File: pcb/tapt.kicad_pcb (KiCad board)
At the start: 4 copper layers, 28.3 x 28.3 mm, 36 parts, among them J1 Conn_01x05_Pin, J2 Conn_01x04_MountingPin, SW1 SW_SPDT_LIMIT, SW2 SW_SPST, U1 nRF52810-QCxx, Y1 32MHz, Y2 32.768kHz

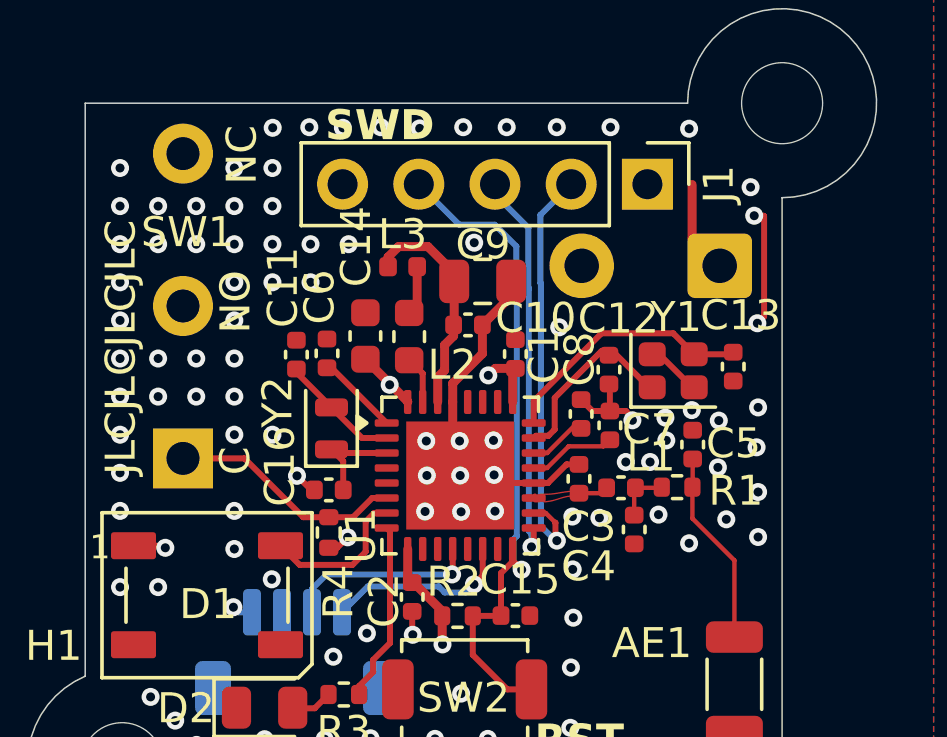
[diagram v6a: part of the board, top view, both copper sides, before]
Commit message: pcb: clock routing improvements
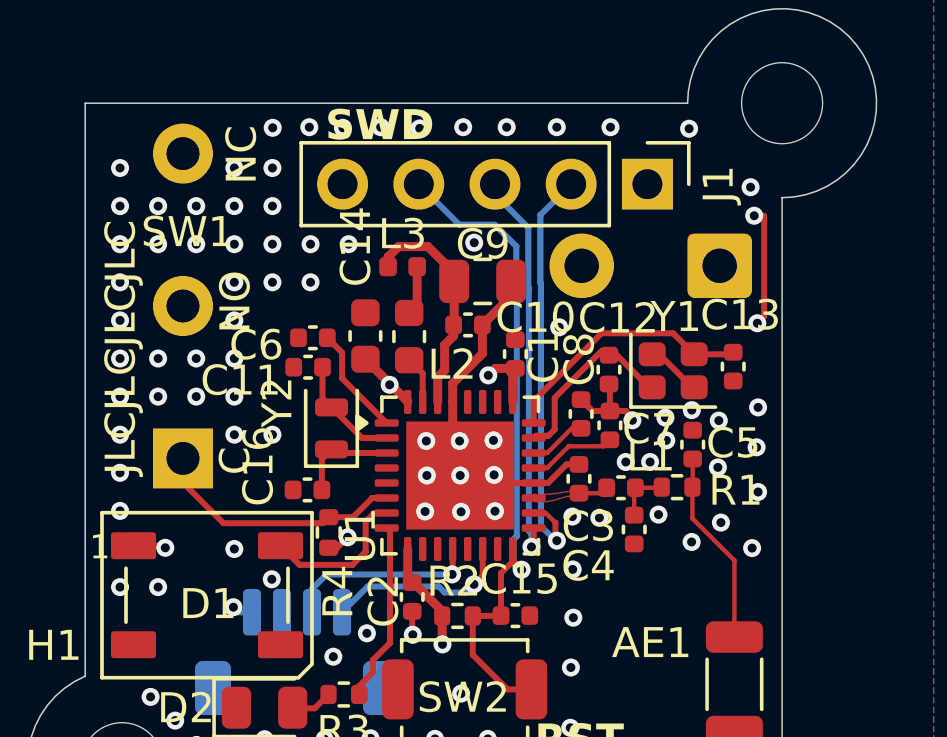
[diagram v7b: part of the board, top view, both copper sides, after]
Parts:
- moved C16 0.71 mm to (93.0, 73.3)
- moved C6 0.70 mm to (93.2, 68.3), turned to 0 degrees
- moved C11 0.57 mm to (93.0, 69.3), turned to 0 degrees
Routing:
- net VDD: track 13.2 -> 11.4 mm
- net Net-(U1-DEC1): track 2.75 -> 3.66 mm
- net GND: track 23.1 -> 22.4 mm, vias 97 -> 95
- net LIMIT: track 7.87 -> 8.51 mm
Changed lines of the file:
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@@
 	(footprint "Capacitor_SMD:C_0402_1005Metric"
 		(layer "F.Cu")
-		(at 93.66 68.8 -90)
+		(at 93.19 68.28)
 		(descr "Capacitor SMD 0402 (1005 Metric), square (rectangular) end terminal, IPC-7351 nominal, (Body size source: IPC-SM-782 page 76, https://www.pcb-3d.com/wordpress/wp-content/uploads/ipc-sm-782a_amendment_1_and_2.pdf), generated with kicad-footprint-generator")
 		(tags "capacitor")
 		(property "Reference" "C6"
-			(at -1.88 0.25 90)
+			(at -1.88 0.25 0)
 			(layer "F.SilkS")
 			(effects
@@
 		)
 		(property "Value" "100nF"
-			(at 0 1.16 90)
+			(at 0 1.16 0)
 			(layer "F.Fab")
 			(effects
@@
 		)
 		(property "Datasheet" "~"
-			(at 0 0 90)
+			(at 0 0 0)
 			(layer "F.Fab")
 			(hide yes)
@@
 		)
 		(property "Description" "Unpolarized capacitor"
-			(at 0 0 90)
+			(at 0 0 0)
 			(layer "F.Fab")
 			(hide yes)
@@
 		)
 		(property "LCSC" "C1525"
-			(at 0 0 270)
+			(at 0 0 0)
 			(unlocked yes)
 			(layer "F.Fab")
@@
 		)
 		(property "KLC_S3.3" ""
-			(at 0 0 270)
+			(at 0 0 0)
 			(unlocked yes)
 			(layer "F.Fab")
@@
 		)
 		(property "KLC_S4.1" ""
-			(at 0 0 270)
+			(at 0 0 0)
 			(unlocked yes)
 			(layer "F.Fab")
@@
 		(attr smd)
 		(fp_line
-			(start -0.107836 0.36)
-			(end 0.107836 0.36)
+			(start -0.107836 -0.36)
+			(end 0.107836 -0.36)
 			(stroke
 				(width 0.12)
@@
 		)
 		(fp_line
-			(start -0.107836 -0.36)
-			(end 0.107836 -0.36)
+			(start -0.107836 0.36)
+			(end 0.107836 0.36)
 			(stroke
 				(width 0.12)
@@
 		)
 		(fp_text user "${REFERENCE}"
-			(at 0 0 90)
+			(at 0 0 0)
 			(layer "F.Fab")
 			(effects
@@
 		)
 		(pad "1" smd roundrect
-			(at -0.48 0 270)
+			(at -0.48 0)
 			(size 0.56 0.62)
 			(layers "F.Cu" "F.Mask" "F.Paste")
@@
 		)
 		(pad "2" smd roundrect
-			(at 0.48 0 270)
+			(at 0.48 0)
 			(size 0.56 0.62)
 			(layers "F.Cu" "F.Mask" "F.Paste")
@@
 	(footprint "Capacitor_SMD:C_0402_1005Metric"
 		(layer "F.Cu")
-		(at 93.72 73.35)
+		(at 93.01 73.35)
 		(descr "Capacitor SMD 0402 (1005 Metric), square (rectangular) end terminal, IPC-7351 nominal, (Body size source: IPC-SM-782 page 76, https://www.pcb-3d.com/wordpress/wp-content/uploads/ipc-sm-782a_amendment_1_and_2.pdf), generated with kicad-footprint-generator")
 		(tags "capacitor")
@@
 	(footprint "Capacitor_SMD:C_0402_1005Metric"
 		(layer "F.Cu")
-		(at 92.64 68.84 -90)
+		(at 93.03 69.26)
 		(descr "Capacitor SMD 0402 (1005 Metric), square (rectangular) end terminal, IPC-7351 nominal, (Body size source: IPC-SM-782 page 76, https://www.pcb-3d.com/wordpress/wp-content/uploads/ipc-sm-782a_amendment_1_and_2.pdf), generated with kicad-footprint-generator")
 		(tags "capacitor")
 		(property "Reference" "C11"
-			(at -2.24 0.45 90)
+			(at -2.24 0.45 0)
 			(layer "F.SilkS")
 			(effects
@@
 		)
 		(property "Value" "12pF"
-			(at 0 1.16 90)
+			(at 0 1.16 0)
 			(layer "F.Fab")
 			(effects
@@
 		)
 		(property "Datasheet" "~"
-			(at 0 0 90)
+			(at 0 0 0)
 			(layer "F.Fab")
 			(hide yes)
@@
 		)
 		(property "Description" "Unpolarized capacitor"
-			(at 0 0 90)
+			(at 0 0 0)
 			(layer "F.Fab")
 			(hide yes)
@@
 		)
 		(property "LCSC" "C1547"
-			(at 0 0 270)
+			(at 0 0 0)
 			(unlocked yes)
 			(layer "F.Fab")
@@
 		)
 		(property "KLC_S3.3" ""
-			(at 0 0 270)
+			(at 0 0 0)
 			(unlocked yes)
 			(layer "F.Fab")
@@
 		)
 		(property "KLC_S4.1" ""
-			(at 0 0 270)
+			(at 0 0 0)
 			(unlocked yes)
 			(layer "F.Fab")
@@
 		(attr smd)
 		(fp_line
-			(start -0.107836 0.36)
-			(end 0.107836 0.36)
+			(start -0.107836 -0.36)
+			(end 0.107836 -0.36)
 			(stroke
 				(width 0.12)
@@
 		)
 		(fp_line
-			(start -0.107836 -0.36)
-			(end 0.107836 -0.36)
+			(start -0.107836 0.36)
+			(end 0.107836 0.36)
 			(stroke
 				(width 0.12)
@@
 		)
 		(fp_text user "${REFERENCE}"
-			(at 0 0 90)
+			(at 0 0 0)
 			(layer "F.Fab")
 			(effects
@@
 		)
 		(pad "1" smd roundrect
-			(at -0.48 0 270)
+			(at -0.48 0)
 			(size 0.56 0.62)
 			(layers "F.Cu" "F.Mask" "F.Paste")
@@
 		)
 		(pad "2" smd roundrect
-			(at 0.48 0 270)
+			(at 0.48 0)
 			(size 0.56 0.62)
 			(layers "F.Cu" "F.Mask" "F.Paste")
@@
 	)
 	(segment
+		(start 92.64 69.32)
+		(end 92.64 69.43)
+		(width 0.2)
+		(layer "F.Cu")
+		(net 3)
+	)
+	(segment
 		(start 103.62 70.72)
 		(end 103.09 70.72)
@@
 	)
 	(segment
-		(start 93.13 73.35)
-		(end 92.66 72.88)
-		(width 0.2)
-		(layer "F.Cu")
-		(net 3)
-	)
-	(segment
 		(start 107.9 67.9)
 		(end 108.005 67.795)
@@
 	)
 	(segment
-		(start 93.24 73.35)
-		(end 93.13 73.35)
-		(width 0.2)
-		(layer "F.Cu")
-		(net 3)
-	)
-	(segment
 		(start 98.84 68.809343)
 		(end 98.84 67.85)
@@
 	)
 	(via
-		(at 106.97 74.33)
+		(at 106.790986 74.439014)
 		(size 0.6)
 		(drill 0.3)
@@
 	)
 	(via
-		(at 90.57119 74.05)
-		(size 0.6)
-		(drill 0.3)
-		(layers "F.Cu" "B.Cu")
-		(free yes)
-		(net 3)
-	)
-	(via
 		(at 89.30119 65.16)
 		(size 0.6)
@@
 	)
 	(via
-		(at 108.03 74.92)
+		(at 107.83 75.29)
 		(size 0.6)
 		(drill 0.3)
@@
 	)
 	(via
-		(at 92.66 72.88)
-		(size 0.6)
-		(drill 0.3)
-		(layers "F.Cu" "B.Cu")
-		(net 3)
-	)
-	(via
 		(at 90.57119 67.7)
 		(size 0.6)
@@
 	)
 	(via
-		(at 105.73 75.13)
+		(at 105.814014 75.085986)
 		(size 0.6)
 		(drill 0.3)
@@
 	)
 	(segment
-		(start 105.83 63.17)
-		(end 105.83 64.96)
-		(width 0.3)
-		(layer "F.Cu")
-		(net 4)
-	)
-	(segment
 		(start 95.7675 69.8225)
 		(end 95.748643 69.841357)
@@
 	)
 	(segment
-		(start 93.66 69.28)
-		(end 93.81 69.28)
+		(start 94.164 68.774)
+		(end 94.164 69.634)
 		(width 0.2)
 		(layer "F.Cu")
@@
 	)
 	(segment
-		(start 93.81 69.28)
+		(start 94.164 69.634)
 		(end 95.65 71.12)
 		(width 0.2)
@@
 	)
 	(segment
+		(start 93.67 68.28)
+		(end 94.164 68.774)
+		(width 0.2)
+		(layer "F.Cu")
+		(net 9)
+	)
+	(segment
 		(start 97.9 66.115926)
 		(end 97.023074 65.239)
@@
 	)
 	(segment
-		(start 92.64 69.32)
-		(end 92.64 69.43)
+		(start 93.51 69.26)
+		(end 93.51 70.3)
 		(width 0.2)
 		(layer "F.Cu")
@@
 	)
 	(segment
-		(start 92.64 69.43)
+		(start 93.51 70.3)
 		(end 93.81 70.6)
 		(width 0.2)
@@
 	)
 	(segment
-		(start 93.72 74.26)
-		(end 92.87 74.26)
+		(start 95.167102 73.62)
+		(end 95.65 73.62)
 		(width 0.2)
 		(layer "F.Cu")
@@
 	)
 	(segment
-		(start 95.167102 73.62)
-		(end 95.65 73.62)
+		(start 88.86 73.11)
+		(end 88.86 72.3)
 		(width 0.2)
 		(layer "F.Cu")
@@
 	)
 	(segment
-		(start 94.527102 74.26)
-		(end 95.167102 73.62)
+		(start 90.209 74.459)
+		(end 88.86 73.11)
 		(width 0.2)
 		(layer "F.Cu")
@@
 	)
 	(segment
-		(start 92.87 74.26)
-		(end 90.91 72.3)
+		(start 93.521 74.459)
+		(end 90.209 74.459)
 		(width 0.2)
 		(layer "F.Cu")
@@
 	)
 	(segment
-		(start 90.91 72.3)
-		(end 88.86 72.3)
+		(start 94.527102 74.26)
+		(end 95.167102 73.62)
+		(width 0.2)
+		(layer "F.Cu")
+		(net 18)
+	)
+	(segment
+		(start 93.72 74.26)
+		(end 93.521 74.459)
 		(width 0.2)
 		(layer "F.Cu")
@@
 	)
 	(segment
-		(start 94.2 72.39)
-		(end 93.81 72)
+		(start 93.93 72.12)
+		(end 95.65 72.12)
 		(width 0.2)
 		(layer "F.Cu")
@@
 	)
 	(segment
-		(start 94.2 73.35)
-		(end 94.2 72.39)
+		(start 93.81 72)
+		(end 93.93 72.12)
 		(width 0.2)
 		(layer "F.Cu")
@@
 	)
 	(segment
-		(start 93.93 72.12)
-		(end 95.65 72.12)
+		(start 93.49 73.35)
+		(end 93.49 72.32)
 		(width 0.2)
 		(layer "F.Cu")
@@
 	)
 	(segment
-		(start 93.81 72)
-		(end 93.93 72.12)
+		(start 93.49 72.32)
+		(end 93.81 72)
 		(width 0.2)
 		(layer "F.Cu")
@@
 		(polygon
 			(pts
-				(xy 103.18 72.53) (xy 103 72.89) (xy 102.576996 72.986548) (xy 102.237772 72.716026) (xy 102.237772 72.282144)
-				(xy 102.576996 72.011622) (xy 103 72.10817)
+				(xy 102.57 72.75) (xy 102.47 72.91) (xy 102.256996 72.986548) (xy 101.917772 72.716026) (xy 101.917772 72.282144)
+				(xy 102.256996 72.011622) (xy 102.55 72.23)
 			)
 		)
@@
 			"394d8c8a-dd6b-4c87-8b4e-98142ac8d941" "3d8690fc-de23-45d0-94f6-2e1b3a80b6c1"
 			"3dc0b03a-ff67-4bf0-85ca-2d25956d144f" "415b4172-8e34-4346-a5c5-1051eb2f3457"
-			"5b86ad54-fa14-42c1-a748-e94901416f2a" "5d32600e-6879-4401-b099-6a89159da2ee"
-			"615a3619-708d-4502-8d74-b7aa7efaea35" "6a367b3d-0043-4cce-8e1f-52d35ba62338"
-			"6d91f0a6-c01e-44af-86f9-0d4b64dbfc3f" "70b135ad-b986-4269-b6f9-5da7b8cac3a0"
-			"7333fc35-924d-4840-92fa-a92772fa5622" "758c8fe8-1e7f-4542-b9b4-f23d3895725b"
-			"785630ad-ac58-4cdb-b5af-da5a4a5baddb" "7b16aa5f-b051-4757-a830-e2beef45a1aa"
-			"7c9397f9-86da-4db2-ac97-652ca41210de" "8e8e7b76-ae7b-4a24-9dcd-7ffe77466d64"
-			"96eed214-d4a0-4f36-a3cd-7206a8a9d089" "9feb2357-0b66-4e82-bd5d-7ee2fbd9d45f"
-			"a598a10a-4723-4f89-aa88-1a0b04a16bf2" "a7303749-ecd1-43a6-aca8-0b0743363f35"
-			"ac3cee97-7bfe-4565-9d93-5d7c506d6d97" "b7a064ec-eba1-4c6a-aef5-37707c0b57c1"
-			"cf2ff0ee-c5cc-40d8-81ca-a6bb954e566d" "d2e89277-f72c-43a6-b8d4-676bbfa7e82a"
-			"d5fe8ae3-d3a3-4ef5-a2d5-cf467fb21f55" "d7f734d0-b082-438e-baf6-68e1a54f13b6"
-			"dc391ced-6002-4562-9dd1-63ed992c9425" "f134cc32-a03e-4154-9756-2d59eb056f0c"
+			"5d32600e-6879-4401-b099-6a89159da2ee" "615a3619-708d-4502-8d74-b7aa7efaea35"
+			"6a367b3d-0043-4cce-8e1f-52d35ba62338" "6d91f0a6-c01e-44af-86f9-0d4b64dbfc3f"
+			"70b135ad-b986-4269-b6f9-5da7b8cac3a0" "7333fc35-924d-4840-92fa-a92772fa5622"
+			"758c8fe8-1e7f-4542-b9b4-f23d3895725b" "785630ad-ac58-4cdb-b5af-da5a4a5baddb"
+			"7b16aa5f-b051-4757-a830-e2beef45a1aa" "7c9397f9-86da-4db2-ac97-652ca41210de"
+			"8e8e7b76-ae7b-4a24-9dcd-7ffe77466d64" "96eed214-d4a0-4f36-a3cd-7206a8a9d089"
+			"9feb2357-0b66-4e82-bd5d-7ee2fbd9d45f" "a598a10a-4723-4f89-aa88-1a0b04a16bf2"
+			"a7303749-ecd1-43a6-aca8-0b0743363f35" "ac3cee97-7bfe-4565-9d93-5d7c506d6d97"
+			"b7a064ec-eba1-4c6a-aef5-37707c0b57c1" "cf2ff0ee-c5cc-40d8-81ca-a6bb954e566d"
+			"d2e89277-f72c-43a6-b8d4-676bbfa7e82a" "d5fe8ae3-d3a3-4ef5-a2d5-cf467fb21f55"
+			"d7f734d0-b082-438e-baf6-68e1a54f13b6" "dc391ced-6002-4562-9dd1-63ed992c9425"
+			"f134cc32-a03e-4154-9756-2d59eb056f0c"
 		)
 	)

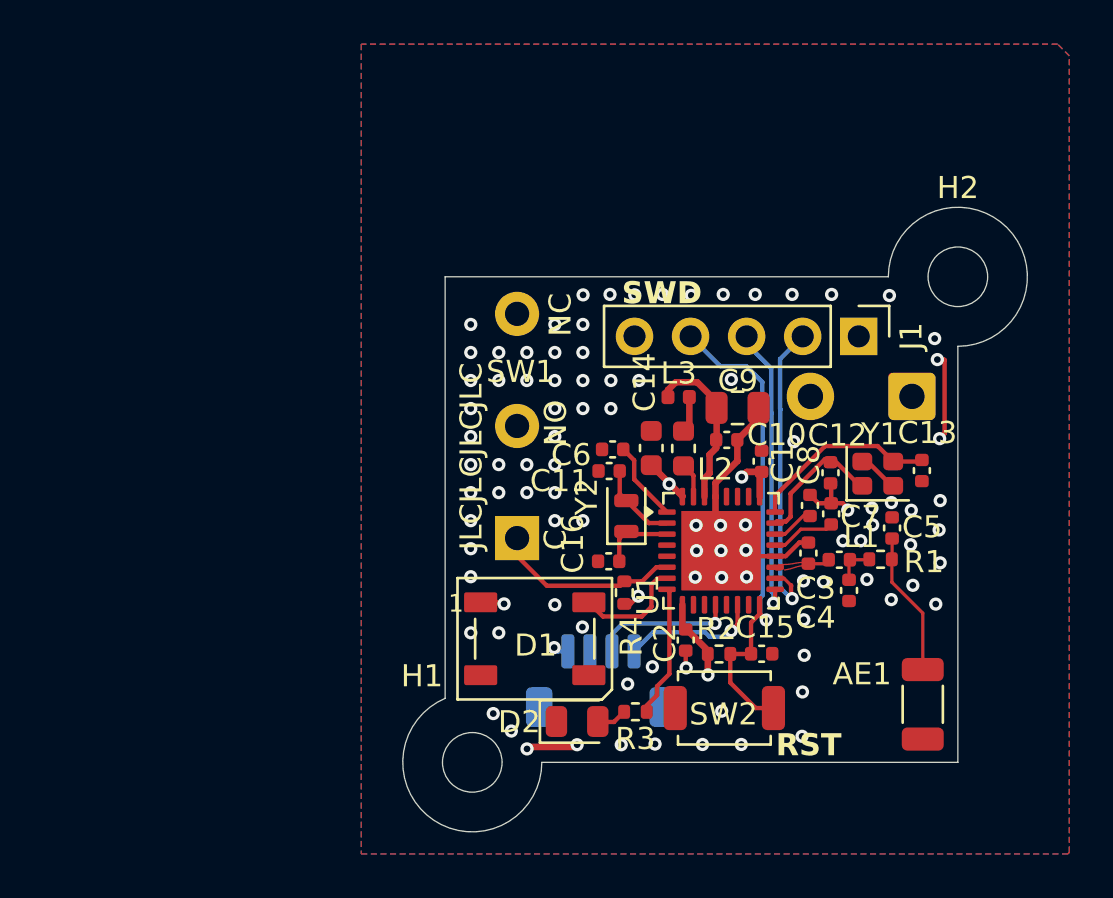
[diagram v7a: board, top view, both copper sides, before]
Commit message: pcb: battery voltagef divider, hf clock routing
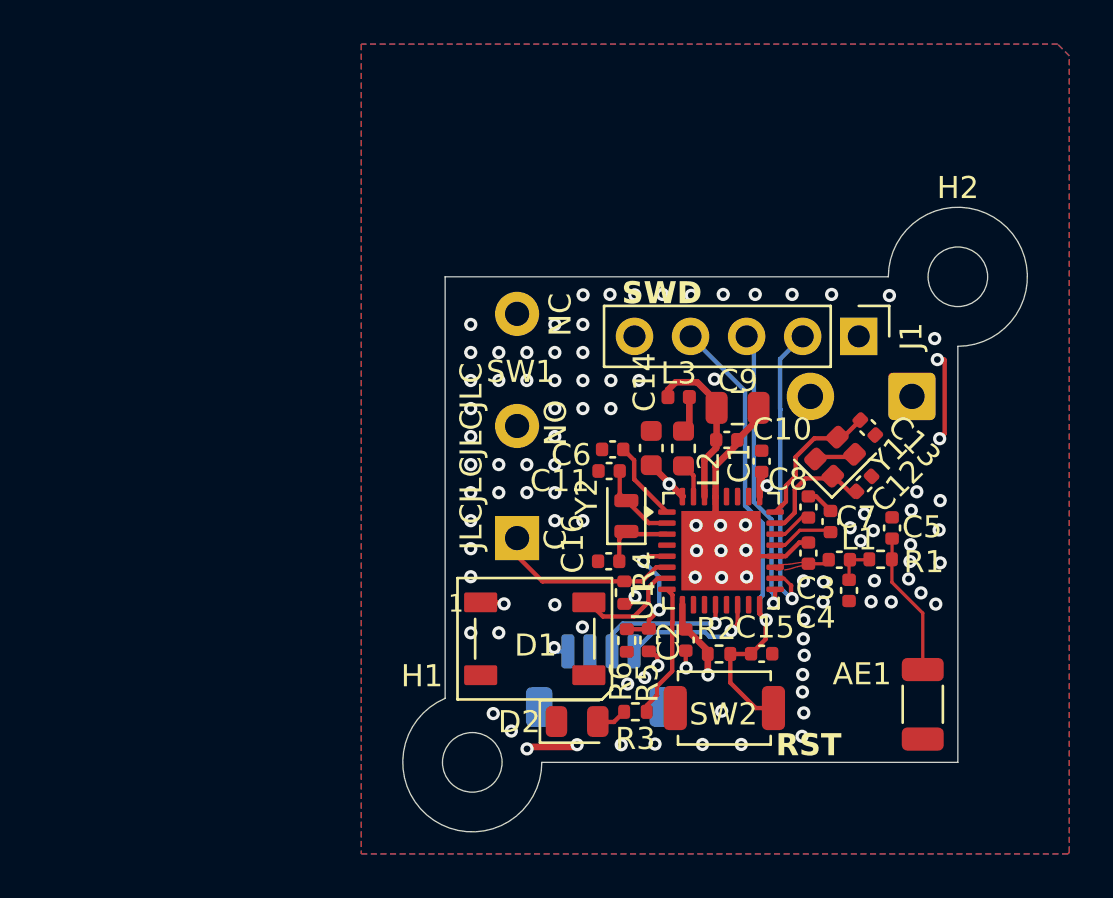
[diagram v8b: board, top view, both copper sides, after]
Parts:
- added R5: 1M, Resistor_SMD:R_0402_1005Metric, F.Cu at (94.8, 76.9)
- added R6: 1M, Resistor_SMD:R_0402_1005Metric, F.Cu at (93.8, 76.9)
- moved C13 3.13 mm to (104.8, 67.3), turned to 135 degrees
- moved Y1 2.08 mm to (103.3, 68.6), turned to 45 degrees
- moved C12 1.60 mm to (104.6, 69.8), turned to -135 degrees
- moved C7 0.35 mm to (103.1, 71.5)
- moved C8 0.10 mm to (102.1, 70.9)
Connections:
- U1 pad 5: unconnected-(U1-P0.05/AIN3-Pad5) -> BAT_MEASURE
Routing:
- net BAT_MEASURE: track 0.00 -> 5.72 mm, vias 0 -> 2
- net XC2: track 8.54 -> 6.51 mm
- net GND: track 22.4 -> 21.1 mm, vias 95 -> 100
- net XC1: track 6.07 -> 5.44 mm
- net VDD: track 11.4 -> 12.0 mm, vias 6 -> 7
